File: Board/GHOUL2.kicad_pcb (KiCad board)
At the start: 2 copper layers, 105.4 x 88.9 mm, 21 parts

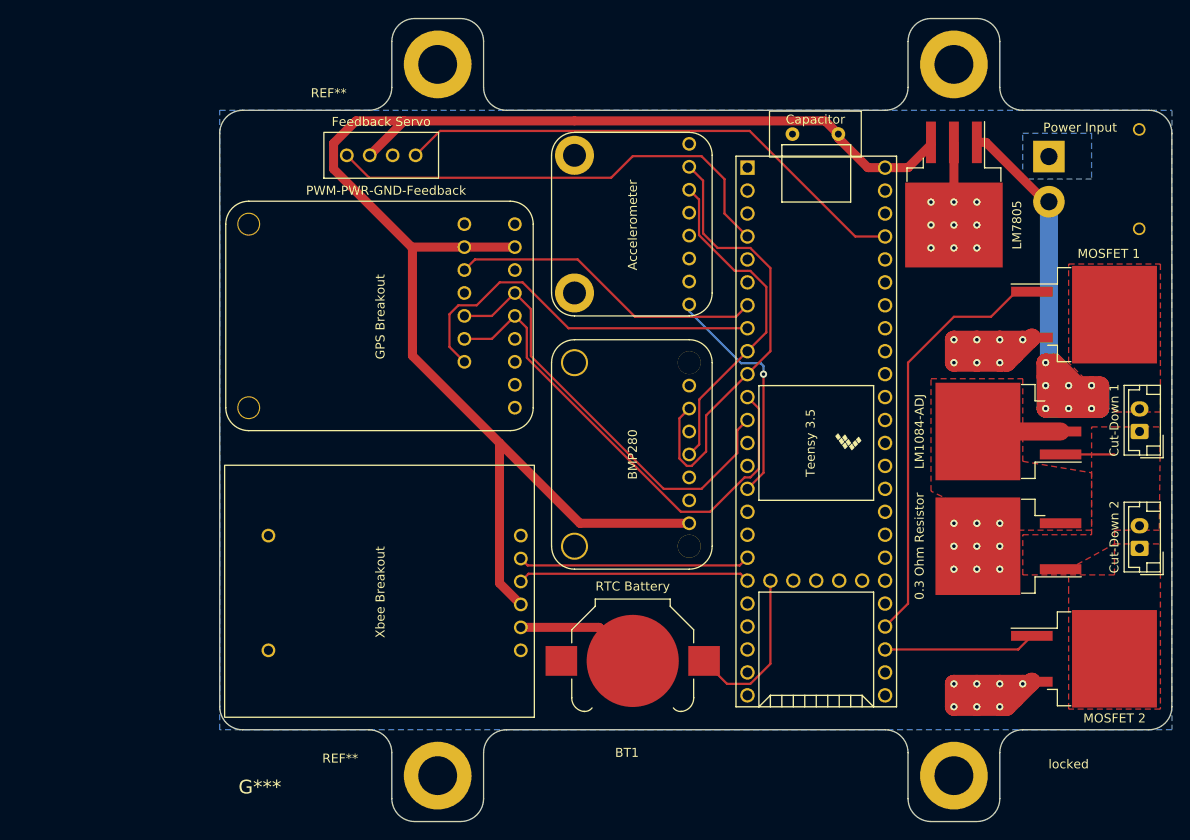
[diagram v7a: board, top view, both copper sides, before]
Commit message: Schematic clarity improvements
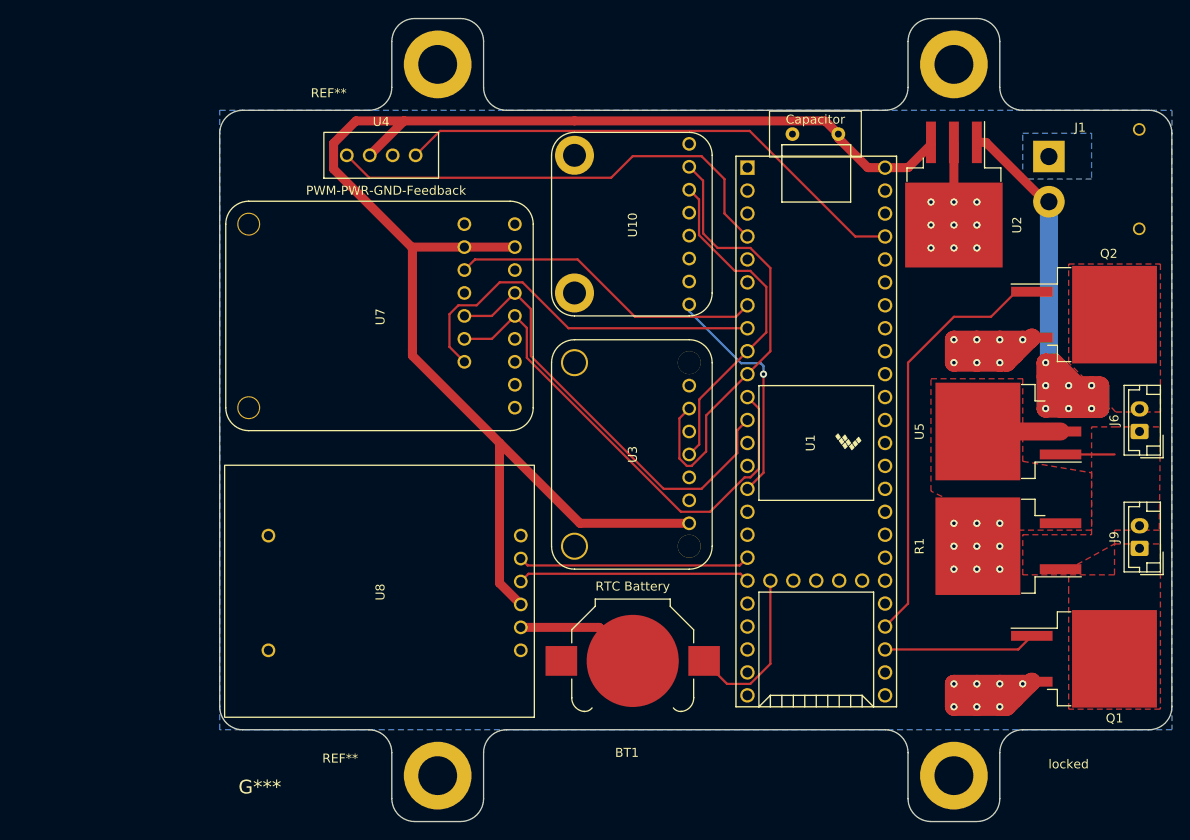
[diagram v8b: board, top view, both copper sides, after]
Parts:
- J1: renamed from Power Input
- J6: renamed from Cut-Down 1; value NichromeConnector -> Nichrome Connector
- J9: renamed from Cut-Down 2; value NichromeConnector -> Nichrome Connector
- Q1: renamed from MOSFET 2
- Q2: renamed from MOSFET 1
- R1: renamed from 0.3 Ohm Resistor
- U1: renamed from Teensy 3.5
- U4: renamed from Feedback Servo
- U7: renamed from GPS Breakout
- U8: renamed from Xbee Breakout
- renumbered Accelerometer to U10, LM7805 to U2, BMP280 to U3, LM1084-ADJ to U5
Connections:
- net 3v3 pwr renamed +3V3
- net Net-(U1-Pad11) renamed TX
- net Net-(U1-Pad12) renamed RX
- net Vin renamed /BATT
- U1 pad 53: 5v pwr -> +5V
- U2 pad 3: 5v pwr -> +5V
- U3 pad 1: 5v pwr -> +5V
- U3 pad 5: (no net) -> unconnected-(U3-Pad5)
- U4 pad 2: 5v pwr -> +5V
- U7 pad 10: unconnected-(U1-Pad8) -> (no net)
- U7 pad 12: unconnected-(U1-Pad7) -> (no net)
- U7 pad 8: 5v pwr -> +5V
- U8 pad 2: 5v pwr -> +5V
- U8 pad 3: Xbee DOut -> Xbee Dout
- U8 pad 4: Xbee DIn -> Xbee Din
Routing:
- net 5v pwr: track 172.1 -> 0.00 mm
- net +5V: track 0.00 -> 172.1 mm
